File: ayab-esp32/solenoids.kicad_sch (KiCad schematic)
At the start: 11 parts, among them U301 MCP23017_SS

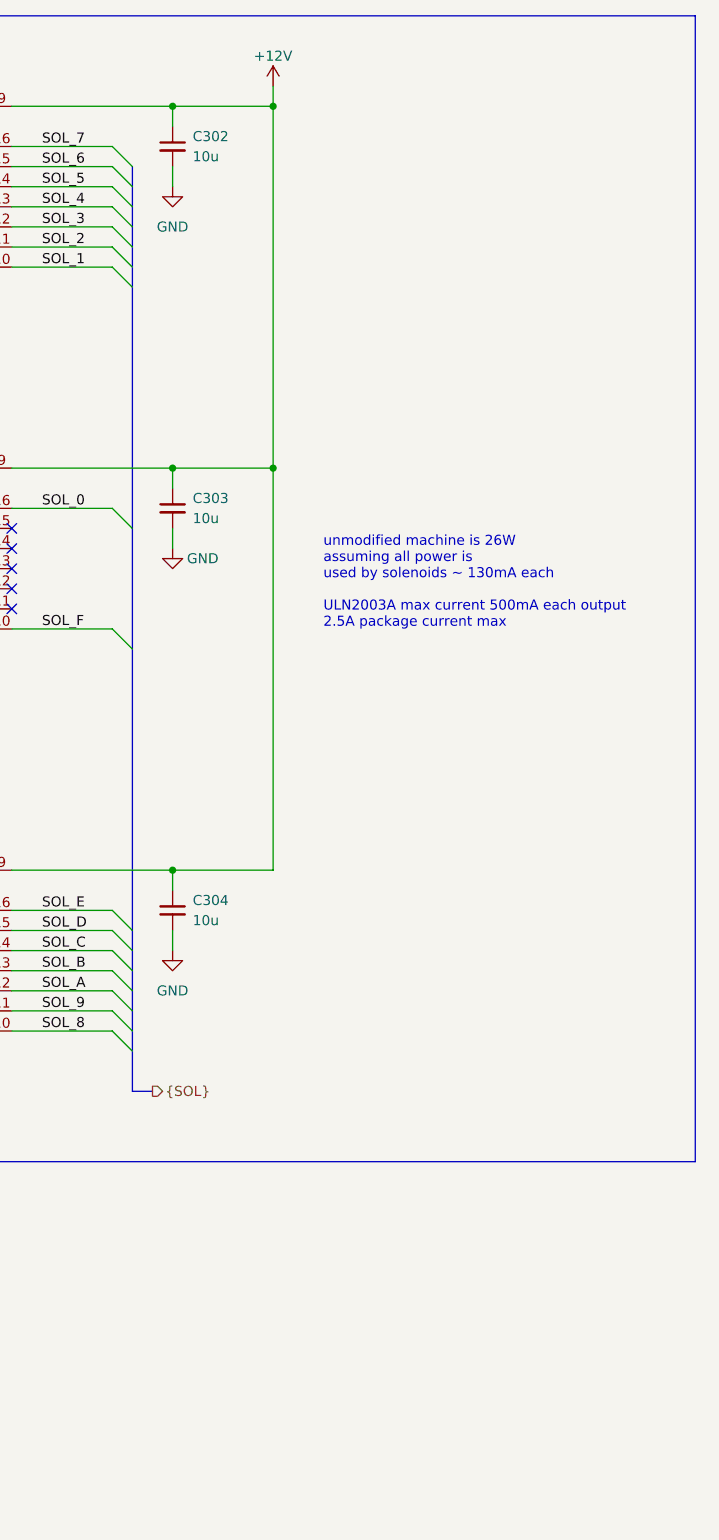
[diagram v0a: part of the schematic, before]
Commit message: Add hardware-default-OFF solenoid power gate
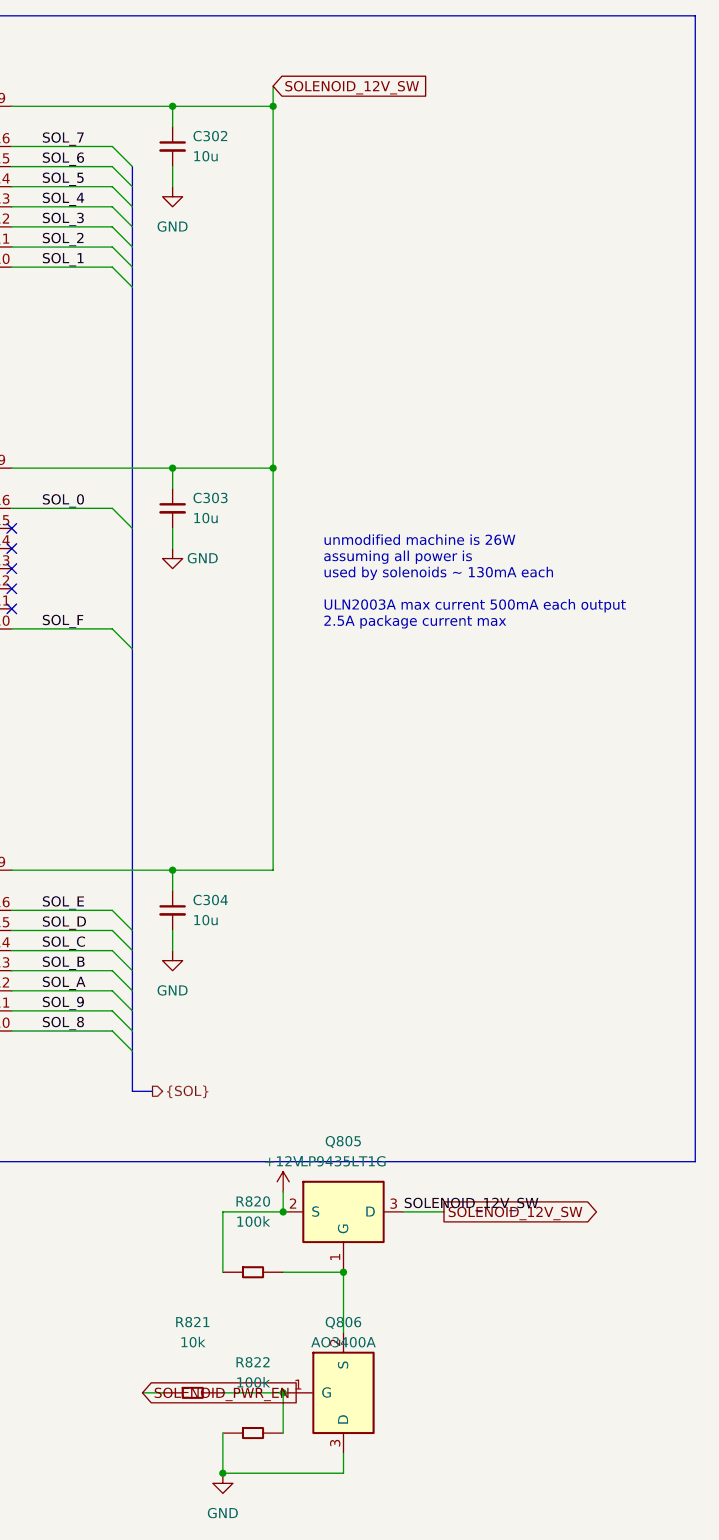
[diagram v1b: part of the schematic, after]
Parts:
- added Q805: LP9435LT1G, Package_TO_SOT_SMD:SOT-23, symbol ayab-lib:LP9435LT1G
- added Q806: AO3400A, Package_TO_SOT_SMD:SOT-23, symbol ayab-lib:AO3400A_FAILSAFE
- added R820, R822: 100k, Resistor_SMD:R_0603_1608Metric, symbol ayab-lib:FAILSAFE_R
- added R821: 10k, Resistor_SMD:R_0603_1608Metric, symbol ayab-lib:FAILSAFE_R
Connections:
- net +12V: now also Q805.2 (S), R820.1; no longer C302.1, C303.1, C304.1, U?.9 (COM), U?.9 (COM), U?.9 (COM)
- net GND: now also Q806.3 (D), R822.1
- new net: Q805.1 (G), Q806.2 (S), R820.2
- new net: Q806.1 (G), R821.2, R822.2
- new net SOLENOID_12V_SW: C302.1, C303.1, C304.1, Q805.3 (D), U?.9 (COM), U?.9 (COM), U?.9 (COM)
- new net SOLENOID_PWR_EN: R821.1

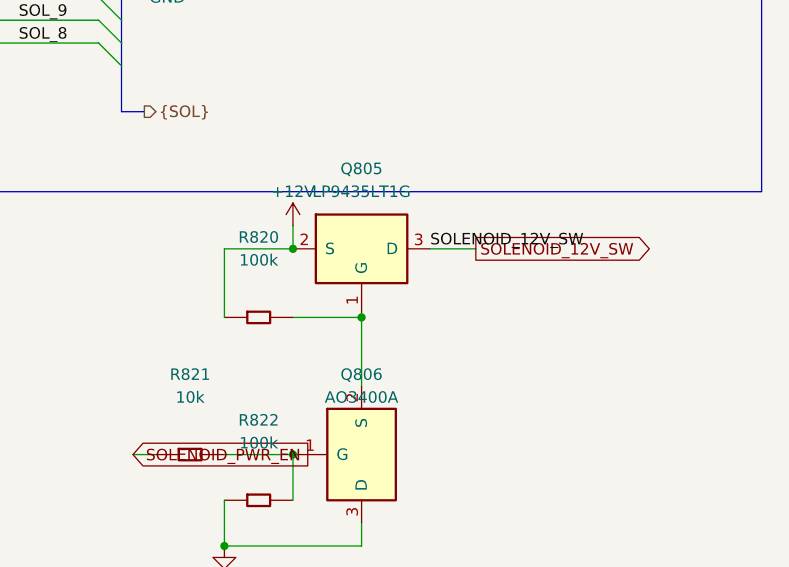
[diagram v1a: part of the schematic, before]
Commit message: Add switched solenoid rail test point
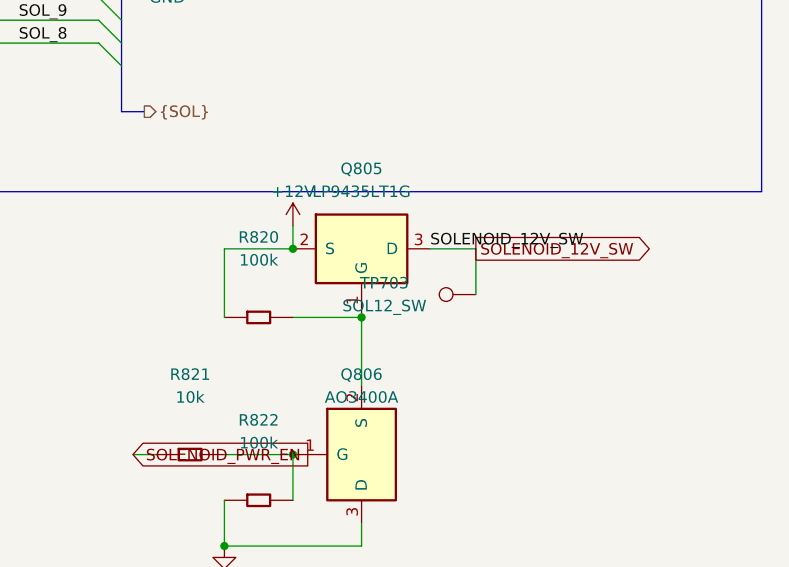
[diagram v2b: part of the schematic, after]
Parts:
- added TP703: SOL12_SW, TestPoint:TestPoint_Pad_D1.0mm, symbol ayab-lib:TestPoint
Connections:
- net SOLENOID_12V_SW: now also TP703.1
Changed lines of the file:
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@@
     (effects (font (size 1.27 1.27)) (justify left))
+  )
+  (wire (pts (xy 248.92 167.64) (xy 248.92 172.72))
+    (stroke (width 0) (type default))
   )
   (wire (pts (xy 228.6 165.1) (xy 228.6 167.64))
@@
         )
       )
+    )
+  )
+(symbol (lib_id "ayab-lib:TestPoint") (at 248.92 172.72 90) (unit 1)
+    (in_bom no) (on_board yes) (dnp no)
+    (property "Reference" "TP703" (at 238.76 171.45 90)
+      (effects (font (size 1.27 1.27)))
+    )
+    (property "Value" "SOL12_SW" (at 238.76 173.99 90)
+      (effects (font (size 1.27 1.27)))
+    )
+    (property "Footprint" "TestPoint:TestPoint_Pad_D1.0mm" (at 248.92 167.64 0)
+      (effects (font (size 1.27 1.27)) hide)
+    )
+    (property "Datasheet" "~" (at 248.92 167.64 0)
+      (effects (font (size 1.27 1.27)) hide)
+    )
+    (property "Package" "" (at 248.92 172.72 0)
+      (effects (font (size 1.27 1.27)) hide)
+    )
+    (property "OEM PN" "" (at 248.92 172.72 0)
+      (effects (font (size 1.27 1.27)) hide)
+    )
+    (property "OEM" "" (at 248.92 172.72 0)
+      (effects (font (size 1.27 1.27)) hide)
+    )
+    (pin "1")
+    (instances
+      (project "ayab-esp32"
+        (path "/ad16b75f-afc8-4717-a7c6-8dd7b69a18e2/5c12a608-dfd1-46fe-96db-4ec512a20774"
+          (reference "TP703") (unit 1)
+        )
+      )

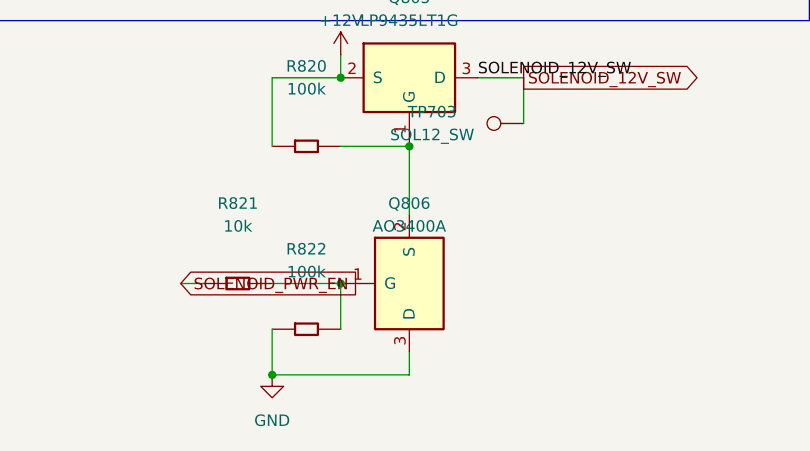
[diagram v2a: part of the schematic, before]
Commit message: Complete corrected solenoid fail-safe schematic
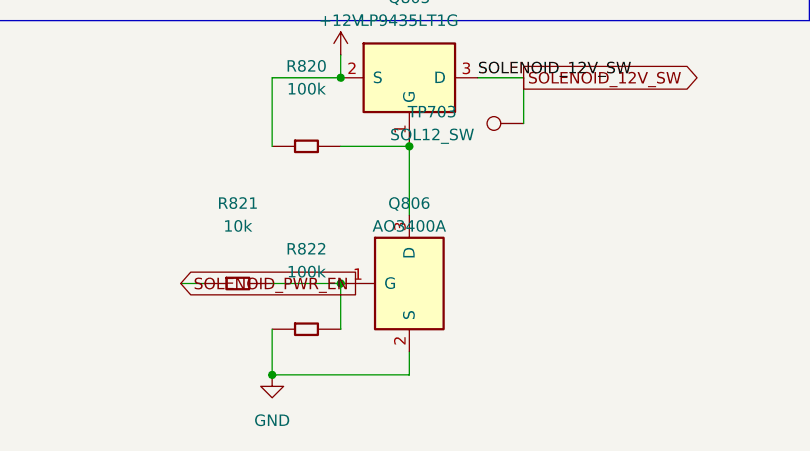
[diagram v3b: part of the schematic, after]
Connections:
- net GND: now also Q806.2 (S); no longer Q806.3 (D)
- net at Q805.1 (G), R820.2: now also Q806.3 (D); no longer Q806.2 (S)
